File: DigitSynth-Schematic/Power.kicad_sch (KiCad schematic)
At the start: 4 parts

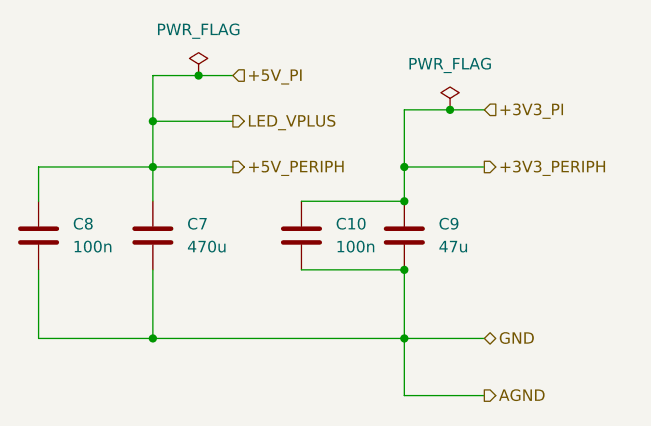
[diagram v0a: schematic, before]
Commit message: removed power schematic sheet as RPI5 has decoupling capacitors; fixed component value errors; buttons removed from RPI5 sheet and added to ADC analog inputs; LED_VPLUS power line removed and replaced by +5V_PERIPH
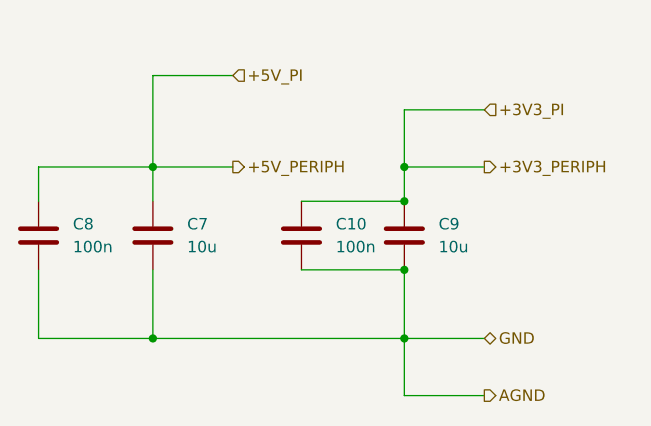
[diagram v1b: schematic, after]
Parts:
- C7: value 470u -> 10u
- C9: value 47u -> 10u
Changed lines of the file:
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@@
-	)
-	(junction
-		(at 152.4 44.45)
-		(diameter 0)
-		(color 0 0 0 0)
-	)
-	(junction
-		(at 147.32 49.53)
-		(diameter 0)
-		(color 0 0 0 0)
 	)
 	(junction
@@
 	)
 	(junction
-		(at 180.34 48.26)
-		(diameter 0)
-		(color 0 0 0 0)
-	)
-	(junction
 		(at 175.26 66.04)
 		(diameter 0)
@@
 	(wire
 		(pts
-			(xy 180.34 48.26) (xy 175.26 48.26)
+			(xy 175.26 48.26) (xy 184.15 48.26)
 		)
 		(stroke
@@
 	(wire
 		(pts
-			(xy 147.32 49.53) (xy 156.21 49.53)
-		)
-		(stroke
-			(width 0)
-			(type default)
-		)
-	)
-	(wire
-		(pts
 			(xy 175.26 73.66) (xy 175.26 80.01)
 		)
@@
 	(wire
 		(pts
-			(xy 147.32 54.61) (xy 147.32 49.53)
+			(xy 147.32 44.45) (xy 147.32 54.61)
 		)
 		(stroke
@@
 	(wire
 		(pts
-			(xy 147.32 44.45) (xy 147.32 49.53)
-		)
-		(stroke
-			(width 0)
-			(type default)
-		)
-	)
-	(wire
-		(pts
 			(xy 147.32 66.04) (xy 147.32 73.66)
 		)
@@
 	(wire
 		(pts
-			(xy 156.21 44.45) (xy 152.4 44.45)
+			(xy 147.32 44.45) (xy 156.21 44.45)
 		)
 		(stroke
@@
 	(wire
 		(pts
-			(xy 184.15 48.26) (xy 180.34 48.26)
-		)
-		(stroke
-			(width 0)
-			(type default)
-		)
-	)
-	(wire
-		(pts
 			(xy 147.32 73.66) (xy 175.26 73.66)
-		)
-		(stroke
-			(width 0)
-			(type default)
-		)
-	)
-	(wire
-		(pts
-			(xy 152.4 44.45) (xy 147.32 44.45)
 		)
 		(stroke
@@
 		)
 	)
-	(hierarchical_label "LED_VPLUS"
-		(shape output)
-		(at 156.21 49.53 0)
-		(effects
-			(font
-				(size 1.27 1.27)
-			)
-			(justify left)
-		)
-	)
 	(hierarchical_label "+3V3_PI"
 		(shape input)
@@
 			)
 			(justify left)
-		)
-	)
-	(symbol
-		(lib_id "power:PWR_FLAG")
-		(at 180.34 48.26 0)
-		(unit 1)
-		(exclude_from_sim no)
-		(in_bom yes)
-		(on_board yes)
-		(dnp no)
-		(fields_autoplaced yes)
-		(property "Reference" "#FLG01"
-			(at 180.34 46.355 0)
-			(effects
-				(font
-					(size 1.27 1.27)
-				)
-				(hide yes)
-			)
-		)
-		(property "Value" "PWR_FLAG"
-			(at 180.34 43.18 0)
-			(effects
-				(font
-					(size 1.27 1.27)
-				)
-			)
-		)
-		(property "Footprint" ""
-			(at 180.34 48.26 0)
-			(effects
-				(font
-					(size 1.27 1.27)
-				)
-				(hide yes)
-			)
-		)
-		(property "Datasheet" "~"
-			(at 180.34 48.26 0)
-			(effects
-				(font
-					(size 1.27 1.27)
-				)
-				(hide yes)
-			)
-		)
-		(property "Description" "Special symbol for telling ERC where power comes from"
-			(at 180.34 48.26 0)
-			(effects
-				(font
-					(size 1.27 1.27)
-				)
-				(hide yes)
-			)
-		)
-		(pin "1"
-		)
-		(instances
-			(project ""
-				(path "/ad908932-4812-48b1-9c87-6bb086cd45d9/0d869e58-12a4-4e2e-93f9-a423c2ddcdac"
-					(reference "#FLG01")
-					(unit 1)
-				)
-			)
 		)
 	)
@@
 	)
 	(symbol
-		(lib_id "power:PWR_FLAG")
-		(at 152.4 44.45 0)
-		(unit 1)
-		(exclude_from_sim no)
-		(in_bom yes)
-		(on_board yes)
-		(dnp no)
-		(fields_autoplaced yes)
-		(property "Reference" "#FLG02"
-			(at 152.4 42.545 0)
-			(effects
-				(font
-					(size 1.27 1.27)
-				)
-				(hide yes)
-			)
-		)
-		(property "Value" "PWR_FLAG"
-			(at 152.4 39.37 0)
-			(effects
-				(font
-					(size 1.27 1.27)
-				)
-			)
-		)
-		(property "Footprint" ""
-			(at 152.4 44.45 0)
-			(effects
-				(font
-					(size 1.27 1.27)
-				)
-				(hide yes)
-			)
-		)
-		(property "Datasheet" "~"
-			(at 152.4 44.45 0)
-			(effects
-				(font
-					(size 1.27 1.27)
-				)
-				(hide yes)
-			)
-		)
-		(property "Description" "Special symbol for telling ERC where power comes from"
-			(at 152.4 44.45 0)
-			(effects
-				(font
-					(size 1.27 1.27)
-				)
-				(hide yes)
-			)
-		)
-		(pin "1"
-		)
-		(instances
-			(project "DigitSynth"
-				(path "/ad908932-4812-48b1-9c87-6bb086cd45d9/0d869e58-12a4-4e2e-93f9-a423c2ddcdac"
-					(reference "#FLG02")
-					(unit 1)
-				)
-			)
-		)
-	)
-	(symbol
 		(lib_id "Device:C")
 		(at 163.83 62.23 0)
@@
 			)
 		)
-		(property "Value" "47u"
+		(property "Value" "10u"
 			(at 179.07 63.4999 0)
 			(effects
@@
 			)
 		)
-		(property "Value" "470u"
+		(property "Value" "10u"
 			(at 151.13 63.4999 0)
 			(effects
